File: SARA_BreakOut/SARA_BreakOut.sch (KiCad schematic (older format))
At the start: 1 part

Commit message: complete SARA breakout for Xplained EXT1
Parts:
- added AE?: Antenna, symbol Antenna
- added C?: 4.7uF, symbol C
- added C?: 22uF, symbol C
- added C?: 10uF, symbol C
- added C?: 100uF, symbol C
- added C?: 100nF, symbol C
- added C?: 10nF, symbol C
- added C?: 68pF, symbol C
- added C?: 15pF, symbol C
- added C? (x4): 47pF, symbol C
- added C? (x12): C, symbol C
- added C? (x2): 60pF, symbol C
- added D? (x4): PESD0402, symbol PESD0402
- added D?: LED, symbol LED
- added J?: USB_B, symbol USB_B
- added J?: Mechanical_slot, symbol SIM_Card
- added J?: SIM_Card_IC, symbol SIM_Card
- added J?: Vin_source, symbol Conn_01x02
- added J?: 3v8 tp, symbol Conn_01x01
- added J?: 1v8 tp, symbol Conn_01x01
- added J?: v_int_tp, symbol Conn_01x01
- added J?: txd_tp, symbol Conn_01x01
- added J?: rxd_tp, symbol Conn_01x01
- added J?: pwr_on_tp, symbol Conn_01x01
- added J?: gpio1_tp, symbol Conn_01x01
- added J?: reset_n_tp, symbol Conn_01x01
- added J?: gpio6_tp, symbol Conn_01x01
- added J?: gpio5_tp, symbol Conn_01x01
- added J?: cur_tp, symbol Conn_01x02
- added J?: Conn_02x10_Odd_Even, symbol Conn_02x10_Odd_Even
- added L?: 1.0uH, symbol L
- added R?: 200K, symbol R
- added R? (x2): 200k, symbol R
- added R?: 100k, symbol R
- added R?: 9.1K, symbol R
- added R?: 3.9K, symbol R
- added R?: 2k, symbol R
- added SW? (x2): SW_Push, symbol SW_Push
- added U? (x2): LSF0108, symbol LSF0108
- added U?: TLV62568A, symbol TLV62568A
- added U?: LT1764AEQ, symbol LT1764AEQ
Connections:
- net labels added: 1v8, 3v8, 5v, GND, VCC, cts, dcd, dsr, dtr, gpio1, gpio5, gpio6, h_cts, h_dcd, h_dsr, h_dtr, h_gpio1, h_gpio6, h_pwr_on, h_reset_n, h_ri, h_rts, h_rxd, h_txd, h_v_int, high_v, main_vin, pwr_on, reset_n, ri, rts, rxd, sim_clk, sim_io, sim_rst, txd, v_int, vsim
- wire segments 0 -> 202
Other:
- moved on the sheet: U?

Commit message: complete SARA breakout for Xplained EXT1
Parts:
- gave numbers to parts that had none: 63
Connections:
- net labels removed: VCC
- wire segments 202 -> 204

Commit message: complete SARA breakout for Xplained EXT1
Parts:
- removed U3: LT1764AEQ, symbol LT1764AEQ
- added R?: 47K, symbol R
- added U?: AP7361, symbol AP7361
- C3: value 10uF -> 1uF
- C4: value 100uF -> 22uF
- R4: value 9.1K -> 41K
- R5: value 3.9K -> 10k
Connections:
- wire segments 204 -> 208
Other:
- moved on the sheet: C3, C4, R4, R5

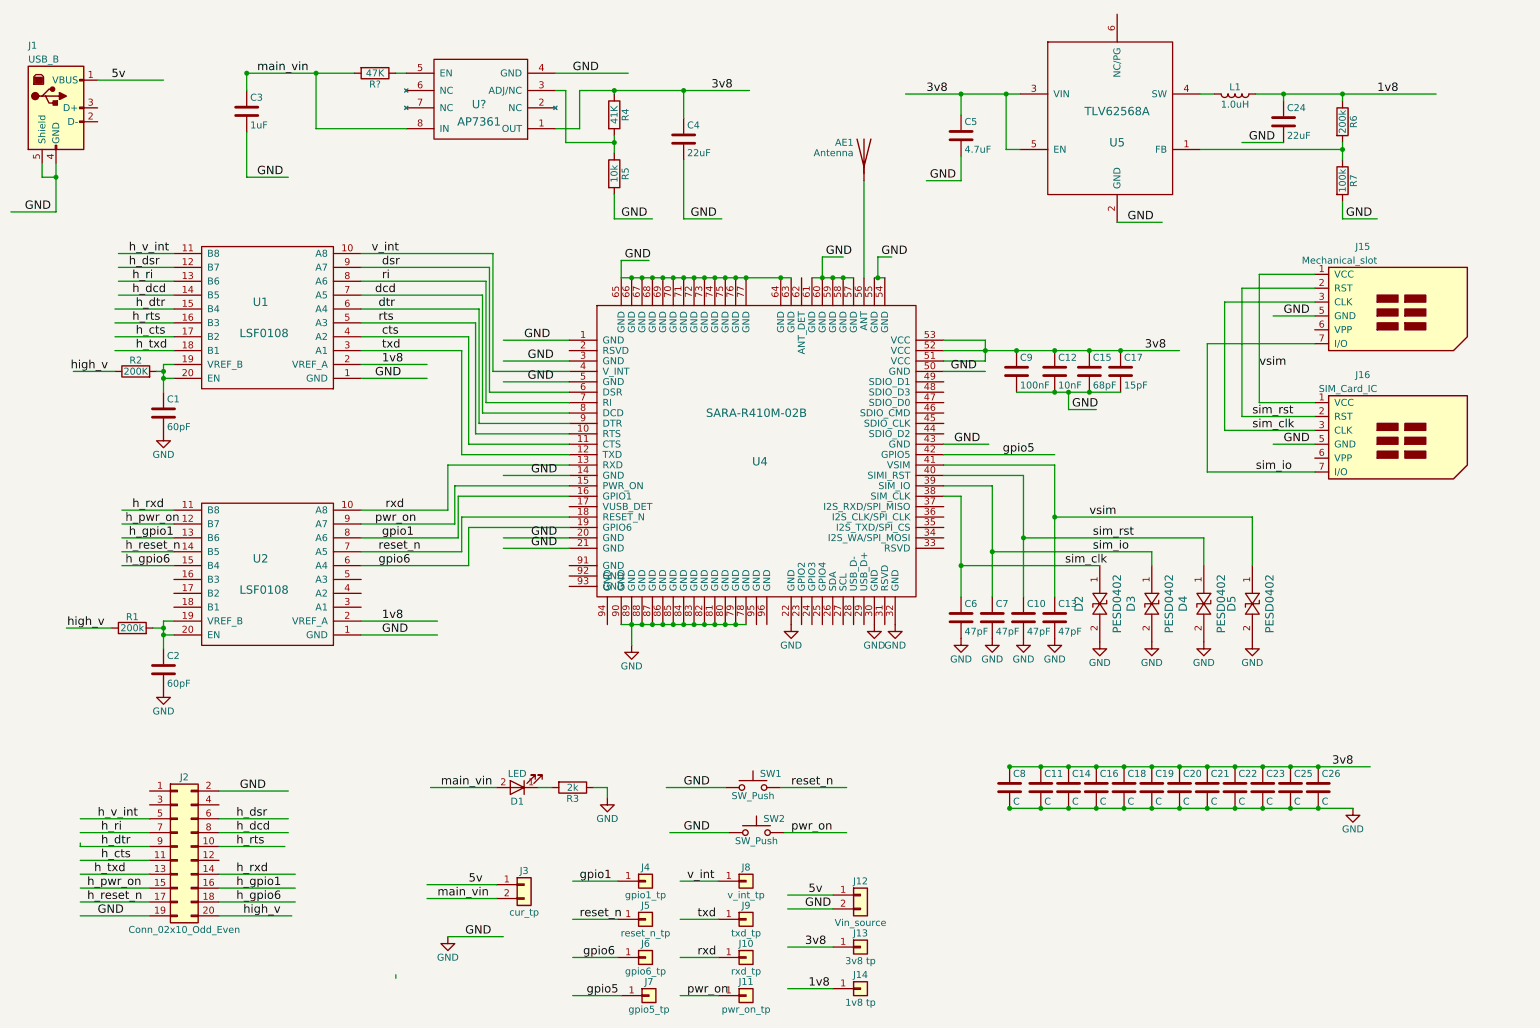
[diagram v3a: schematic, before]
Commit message: breakout board, without sim footprint check, no LED and board VCC
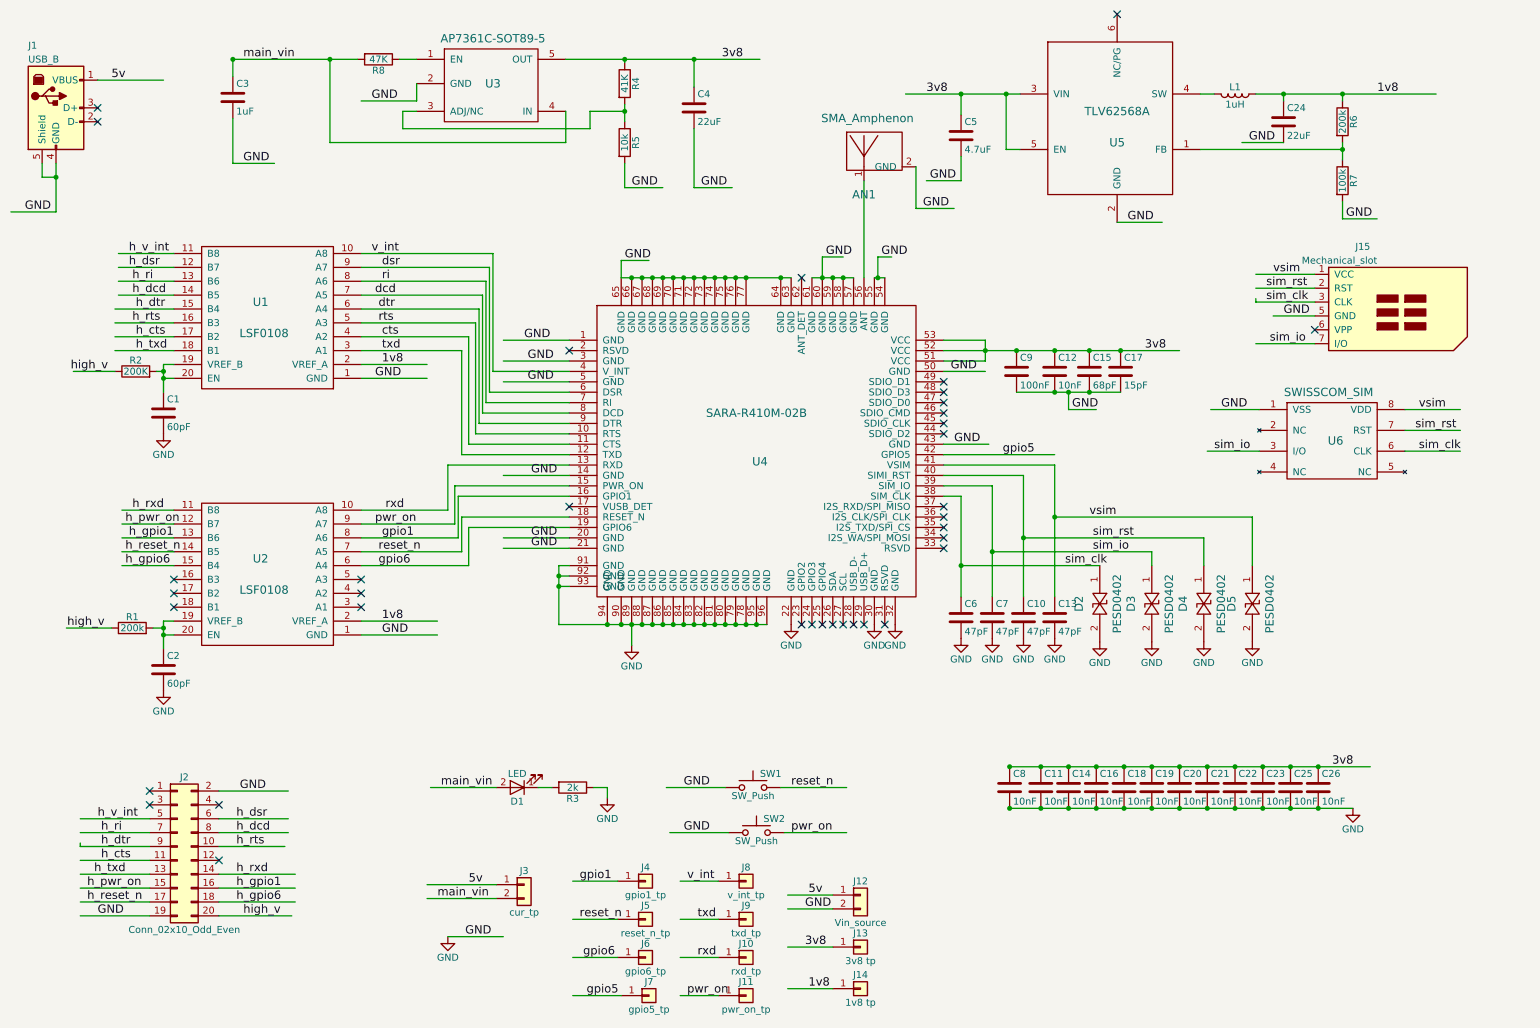
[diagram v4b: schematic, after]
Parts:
- removed AE1: Antenna, symbol Antenna
- removed J16: SIM_Card_IC, symbol SIM_Card
- removed U?: AP7361, symbol AP7361
- added AN1: SMA_Amphenon, SMA:SMA_TH_Amphenol, symbol SMA_Amphenon
- added U3: AP7361C-SOT89-5, TO_SOT_Packages_SMD:SOT-89-5_Housing, symbol AP7361C-SOT89-5
- added U6: SWISSCOM_SIM, SIM_CARD:SWISS_COM_SIMCARD, symbol SWISSCOM_SIM
- C1, C10, C12, C13, C15, C17, C2, C24, C3, C4, C5, C6, C7, C9: footprint (none) -> Capacitors_SMD:C_1206_HandSoldering
- C11, C14, C16, C18, C19, C20, C21, C22, C23, C25, C26, C8: value C -> 10nF; footprint (none) -> Capacitors_SMD:C_1206_HandSoldering
- D1: footprint (none) -> LEDs:LED_1206_HandSoldering
- D2, D3, D4, D5: footprint (none) -> LEDs:LED_0402
- J1: footprint (none) -> Connectors:USB_Micro-B
- J10, J11, J13, J14, J4, J5, J6, J7, J8, J9: footprint (none) -> Pin_Headers:Pin_Header_Straight_1x01_Pitch2.54mm
- J12, J3: footprint (none) -> Pin_Headers:Pin_Header_Straight_1x02_Pitch2.54mm
- J15: footprint (none) -> SIM_CARD:sim7100_9
- J2: footprint (none) -> pin_header:right_side_2x10
- L1: value 1.0uH -> 1uH; footprint (none) -> Inductors_SMD:L_1206_HandSoldering
- R1, R2, R3, R4, R5, R6, R7: footprint (none) -> Resistors_SMD:R_1206_HandSoldering
- R8: renamed from R?; footprint (none) -> Resistors_SMD:R_1206_HandSoldering
- SW1, SW2: footprint (none) -> Buttons_Switches_SMD:SW_SPST_EVQQ2
- U1, U2: footprint (none) -> Housings_SSOP:TSSOP-20_4.4x6.5mm_Pitch0.65mm
- U4: footprint (none) -> uBlox:uBlox_SARA-R4
- U5: footprint (none) -> sot:SOT563
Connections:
- wire segments 208 -> 212
- no-connect marks 0 -> 36
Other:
- moved on the sheet: C3, C4, R4, R5, R8

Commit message: final schem, before starting pcb
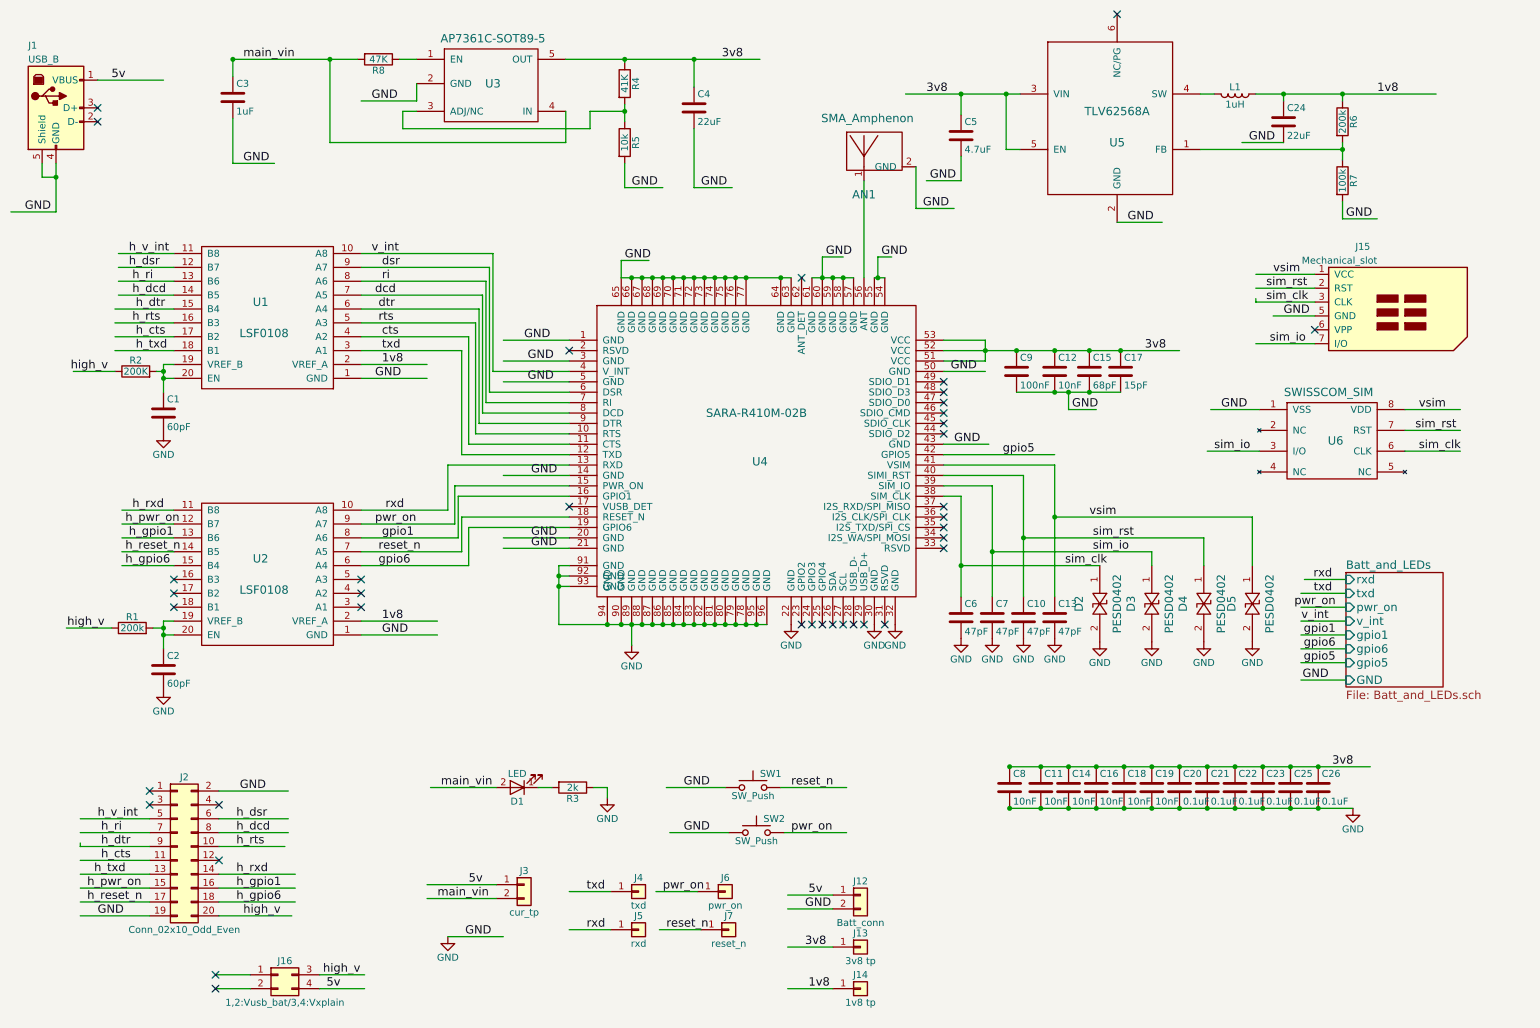
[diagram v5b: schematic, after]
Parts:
- removed J10: rxd_tp, Pin_Headers:Pin_Header_Straight_1x01_Pitch2.54mm, symbol Conn_01x01
- removed J11: pwr_on_tp, Pin_Headers:Pin_Header_Straight_1x01_Pitch2.54mm, symbol Conn_01x01
- removed J8: v_int_tp, Pin_Headers:Pin_Header_Straight_1x01_Pitch2.54mm, symbol Conn_01x01
- removed J9: txd_tp, Pin_Headers:Pin_Header_Straight_1x01_Pitch2.54mm, symbol Conn_01x01
- added J16: 1,2:Vusb_bat/3,4:Vxplain, Pin_Headers:Pin_Header_Angled_2x02_Pitch2.54mm, symbol Conn_02x02_Top_Bottom
- C20, C21, C22, C23, C25, C26: value 10nF -> 0.1uF
- J12: value Vin_source -> Batt_conn
- J4: value gpio1_tp -> txd
- J5: value reset_n_tp -> rxd
- J6: value gpio6_tp -> pwr_on
- J7: value gpio5_tp -> reset_n
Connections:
- wire segments 212 -> 220
- no-connect marks 36 -> 38

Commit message: first finish of pcb
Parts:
- J12: footprint Pin_Headers:Pin_Header_Straight_1x02_Pitch2.54mm -> Pin_Headers:Pin_Header_Angled_1x02_Pitch2.54mm
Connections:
- wire segments 220 -> 212
- no-connect marks 38 -> 39
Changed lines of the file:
@@
 sim_clk
 $Comp
-L GND #PWR9
+L GND #PWR01
 U 1 1 5B1D40A3
 P 7375 5000
-F 0 "#PWR9" H 7375 4750 50  0001 C CNN
+F 0 "#PWR01" H 7375 4750 50  0001 C CNN
 F 1 "GND" H 7375 4850 50  0000 C CNN
 F 2 "" H 7375 5000 50  0001 C CNN
@@
 $EndComp
 $Comp
-L GND #PWR10
+L GND #PWR02
 U 1 1 5B1D4135
 P 7600 5000
-F 0 "#PWR10" H 7600 4750 50  0001 C CNN
+F 0 "#PWR02" H 7600 4750 50  0001 C CNN
 F 1 "GND" H 7600 4850 50  0000 C CNN
 F 2 "" H 7600 5000 50  0001 C CNN
@@
 $EndComp
 $Comp
-L GND #PWR11
+L GND #PWR03
 U 1 1 5B1D41A0
 P 7825 5000
-F 0 "#PWR11" H 7825 4750 50  0001 C CNN
+F 0 "#PWR03" H 7825 4750 50  0001 C CNN
 F 1 "GND" H 7825 4850 50  0000 C CNN
 F 2 "" H 7825 5000 50  0001 C CNN
@@
 $EndComp
 $Comp
-L GND #PWR12
+L GND #PWR04
 U 1 1 5B1D420B
 P 8050 5000
-F 0 "#PWR12" H 8050 4750 50  0001 C CNN
+F 0 "#PWR04" H 8050 4750 50  0001 C CNN
 F 1 "GND" H 8050 4850 50  0000 C CNN
 F 2 "" H 8050 5000 50  0001 C CNN
@@
 $EndComp
 $Comp
-L GND #PWR13
+L GND #PWR05
 U 1 1 5B1D4276
 P 8375 5025
-F 0 "#PWR13" H 8375 4775 50  0001 C CNN
+F 0 "#PWR05" H 8375 4775 50  0001 C CNN
 F 1 "GND" H 8375 4875 50  0000 C CNN
 F 2 "" H 8375 5025 50  0001 C CNN
@@
 $EndComp
 $Comp
-L GND #PWR14
+L GND #PWR06
 U 1 1 5B1D42E1
 P 8750 5025
-F 0 "#PWR14" H 8750 4775 50  0001 C CNN
+F 0 "#PWR06" H 8750 4775 50  0001 C CNN
 F 1 "GND" H 8750 4875 50  0000 C CNN
 F 2 "" H 8750 5025 50  0001 C CNN
@@
 $EndComp
 $Comp
-L GND #PWR15
+L GND #PWR07
 U 1 1 5B1D434C
 P 9125 5025
-F 0 "#PWR15" H 9125 4775 50  0001 C CNN
+F 0 "#PWR07" H 9125 4775 50  0001 C CNN
 F 1 "GND" H 9125 4875 50  0000 C CNN
 F 2 "" H 9125 5025 50  0001 C CNN
@@
 $EndComp
 $Comp
-L GND #PWR16
+L GND #PWR08
 U 1 1 5B1D43B7
 P 9475 5025
-F 0 "#PWR16" H 9475 4775 50  0001 C CNN
+F 0 "#PWR08" H 9475 4775 50  0001 C CNN
 F 1 "GND" H 9475 4875 50  0000 C CNN
 F 2 "" H 9475 5025 50  0001 C CNN
@@
 $EndComp
 $Comp
-L GND #PWR5
+L GND #PWR09
 U 1 1 5B1D5145
 P 5000 5050
-F 0 "#PWR5" H 5000 4800 50  0001 C CNN
+F 0 "#PWR09" H 5000 4800 50  0001 C CNN
 F 1 "GND" H 5000 4900 50  0000 C CNN
 F 2 "" H 5000 5050 50  0001 C CNN
@@
 $EndComp
 $Comp
-L GND #PWR8
+L GND #PWR010
 U 1 1 5B1D53CC
 P 6900 4900
-F 0 "#PWR8" H 6900 4650 50  0001 C CNN
+F 0 "#PWR010" H 6900 4650 50  0001 C CNN
 F 1 "GND" H 6900 4750 50  0000 C CNN
 F 2 "" H 6900 4900 50  0001 C CNN
@@
 $EndComp
 $Comp
-L GND #PWR7
+L GND #PWR011
 U 1 1 5B1D5437
 P 6750 4900
-F 0 "#PWR7" H 6750 4650 50  0001 C CNN
+F 0 "#PWR011" H 6750 4650 50  0001 C CNN
 F 1 "GND" H 6750 4750 50  0000 C CNN
 F 2 "" H 6750 4900 50  0001 C CNN
@@
 $EndComp
 $Comp
-L GND #PWR6
+L GND #PWR012
 U 1 1 5B1D54A2
 P 6150 4900
-F 0 "#PWR6" H 6150 4650 50  0001 C CNN
+F 0 "#PWR012" H 6150 4650 50  0001 C CNN
 F 1 "GND" H 6150 4750 50  0000 C CNN
 F 2 "" H 6150 4900 50  0001 C CNN
@@
 $EndComp
 $Comp
-L GND #PWR17
+L GND #PWR013
 U 1 1 5B1DC5FA
 P 10200 6225
-F 0 "#PWR17" H 10200 5975 50  0001 C CNN
+F 0 "#PWR013" H 10200 5975 50  0001 C CNN
 F 1 "GND" H 10200 6075 50  0000 C CNN
 F 2 "" H 10200 6225 50  0001 C CNN
@@
 $EndComp
 $Comp
-L GND #PWR3
+L GND #PWR014
 U 1 1 5B1DC866
 P 3675 7150
-F 0 "#PWR3" H 3675 6900 50  0001 C CNN
+F 0 "#PWR014" H 3675 6900 50  0001 C CNN
 F 1 "GND" H 3675 7000 50  0000 C CNN
 F 2 "" H 3675 7150 50  0001 C CNN
@@
 $EndComp
 $Comp
-L GND #PWR4
+L GND #PWR015
 U 1 1 5B1E1DBD
 P 4825 6150
-F 0 "#PWR4" H 4825 5900 50  0001 C CNN
+F 0 "#PWR015" H 4825 5900 50  0001 C CNN
 F 1 "GND" H 4825 6000 50  0000 C CNN
 F 2 "" H 4825 6150 50  0001 C CNN
@@
 F 0 "J12" H 6650 6950 50  0000 C CNN
 F 1 "Batt_conn" H 6650 6650 50  0000 C CNN
-F 2 "Pin_Headers:Pin_Header_Straight_1x02_Pitch2.54mm" H 6650 6850 50  0001 C CNN
+F 2 "Pin_Headers:Pin_Header_Angled_1x02_Pitch2.54mm" H 6650 6850 50  0001 C CNN
 F 3 "" H 6650 6850 50  0001 C CNN
 	1    6650 6850
@@
 $EndComp
 $Comp
-L GND #PWR1
+L GND #PWR016
 U 1 1 5B1FEECF
 P 1625 3525
-F 0 "#PWR1" H 1625 3275 50  0001 C CNN
+F 0 "#PWR016" H 1625 3275 50  0001 C CNN
 F 1 "GND" H 1625 3375 50  0000 C CNN
 F 2 "" H 1625 3525 50  0001 C CNN
@@
 $EndComp
 $Comp
-L GND #PWR2
+L GND #PWR017
 U 1 1 5B1FF18D
 P 1625 5375
-F 0 "#PWR2" H 1625 5125 50  0001 C CNN
+F 0 "#PWR017" H 1625 5125 50  0001 C CNN
 F 1 "GND" H 1625 5225 50  0000 C CNN
 F 2 "" H 1625 5375 50  0001 C CNN
@@
 F0 "Batt_and_LEDs" 60
 F1 "Batt_and_LEDs.sch" 60
-F2 "rxd" I L 10150 4575 60
-F3 "txd" I L 10150 4675 60
-F4 "pwr_on" I L 10150 4775 60
-F5 "v_int" I L 10150 4875 60
-F6 "gpio1" I L 10150 4975 60
-F7 "gpio6" I L 10150 5075 60
-F8 "gpio5" I L 10150 5175 60
-F9 "GND" I L 10150 5300 60
 $EndSheet
 $Comp
@@
 Text Label 4675 7100 0    60   ~ 0
 rxd
-Wire Wire Line
-	10150 4575 9850 4575
-Wire Wire Line
-	10150 4675 9825 4675
-Wire Wire Line
-	10150 4775 9825 4775
-Wire Wire Line
-	10150 4875 9825 4875
-Wire Wire Line
-	10150 4975 9825 4975
-Wire Wire Line
-	10150 5075 9825 5075
-Wire Wire Line
-	10150 5175 9825 5175
-Wire Wire Line
-	10150 5300 9825 5300
-Text Label 10050 4575 2    60   ~ 0
-rxd
-Text Label 10050 4675 2    60   ~ 0
-txd
-Text Label 10075 4775 2    60   ~ 0
-pwr_on
-Text Label 10025 4875 2    60   ~ 0
-v_int
-Text Label 10075 4975 2    60   ~ 0
-gpio1
-Text Label 10075 5075 2    60   ~ 0
-gpio6
-Text Label 10075 5175 2    60   ~ 0
-gpio5
-Text Label 10025 5300 2    60   ~ 0
-GND
+NoConn ~ 8050 3675
 $EndSCHEMATC

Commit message: final version 1
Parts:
- removed C14, C16, C18: 10nF, Capacitors_SMD:C_1206_HandSoldering, symbol C
- removed C20, C21, C25: 0.1uF, Capacitors_SMD:C_1206_HandSoldering, symbol C
- removed C9: 100nF, Capacitors_SMD:C_1206_HandSoldering, symbol C
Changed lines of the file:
@@
 3v8
-$Comp
-L C C9
-U 1 1 5B1CA0DF
-P 7775 3075
-F 0 "C9" H 7800 3175 50  0000 L CNN
-F 1 "100nF" H 7800 2975 50  0000 L CNN
-F 2 "Capacitors_SMD:C_1206_HandSoldering" H 7813 2925 50  0001 C CNN
-F 3 "" H 7775 3075 50  0001 C CNN
-	1    7775 3075
-	1    0    0    -1
-$EndComp
 $Comp
 L C C12
@@
 $EndComp
 $Comp
-L C C14
-U 1 1 5B1D7EAB
-P 8150 6075
-F 0 "C14" H 8175 6175 50  0000 L CNN
-F 1 "10nF" H 8175 5975 50  0000 L CNN
-F 2 "Capacitors_SMD:C_1206_HandSoldering" H 8188 5925 50  0001 C CNN
-F 3 "" H 8150 6075 50  0001 C CNN
-	1    8150 6075
-	1    0    0    -1
-$EndComp
-$Comp
-L C C16
-U 1 1 5B1D801C
-P 8350 6075
-F 0 "C16" H 8375 6175 50  0000 L CNN
-F 1 "10nF" H 8375 5975 50  0000 L CNN
-F 2 "Capacitors_SMD:C_1206_HandSoldering" H 8388 5925 50  0001 C CNN
-F 3 "" H 8350 6075 50  0001 C CNN
-	1    8350 6075
-	1    0    0    -1
-$EndComp
-$Comp
-L C C18
-U 1 1 5B1D8081
-P 8550 6075
-F 0 "C18" H 8575 6175 50  0000 L CNN
-F 1 "10nF" H 8575 5975 50  0000 L CNN
-F 2 "Capacitors_SMD:C_1206_HandSoldering" H 8588 5925 50  0001 C CNN
-F 3 "" H 8550 6075 50  0001 C CNN
-	1    8550 6075
-	1    0    0    -1
-$EndComp
-$Comp
 L C C19
 U 1 1 5B1D80DC
@@
 $EndComp
 $Comp
-L C C20
-U 1 1 5B1D813F
-P 8950 6075
-F 0 "C20" H 8975 6175 50  0000 L CNN
-F 1 "0.1uF" H 8975 5975 50  0000 L CNN
-F 2 "Capacitors_SMD:C_1206_HandSoldering" H 8988 5925 50  0001 C CNN
-F 3 "" H 8950 6075 50  0001 C CNN
-	1    8950 6075
-	1    0    0    -1
-$EndComp
-$Comp
-L C C21
-U 1 1 5B1D81AA
-P 9150 6075
-F 0 "C21" H 9175 6175 50  0000 L CNN
-F 1 "0.1uF" H 9175 5975 50  0000 L CNN
-F 2 "Capacitors_SMD:C_1206_HandSoldering" H 9188 5925 50  0001 C CNN
-F 3 "" H 9150 6075 50  0001 C CNN
-	1    9150 6075
-	1    0    0    -1
-$EndComp
-$Comp
 L C C22
 U 1 1 5B1D8211
@@
 F 3 "" H 9550 6075 50  0001 C CNN
 	1    9550 6075
-	1    0    0    -1
-$EndComp
-$Comp
-L C C25
-U 1 1 5B1D82E5
-P 9750 6075
-F 0 "C25" H 9775 6175 50  0000 L CNN
-F 1 "0.1uF" H 9775 5975 50  0000 L CNN
-F 2 "Capacitors_SMD:C_1206_HandSoldering" H 9788 5925 50  0001 C CNN
-F 3 "" H 9750 6075 50  0001 C CNN
-	1    9750 6075
 	1    0    0    -1
 $EndComp
@@
 Connection ~ 8050 2925
 Connection ~ 8300 2925
-Wire Wire Line
-	7775 3225 8525 3225
 Connection ~ 8050 3225
 Connection ~ 8300 3225
@@
 rxd
 NoConn ~ 8050 3675
+Wire Wire Line
+	8050 3225 8525 3225
 $EndSCHEMATC
